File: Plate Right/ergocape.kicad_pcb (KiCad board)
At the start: 2 copper layers, 183.2 x 140.8 mm, 43 parts

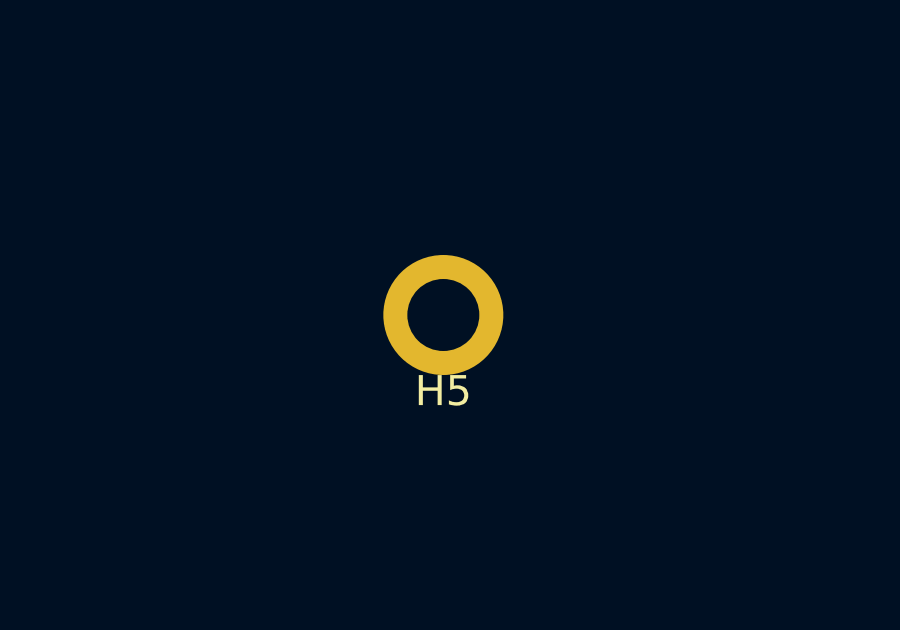
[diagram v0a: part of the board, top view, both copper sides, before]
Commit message: Change in layout and design, remove atmega32u4
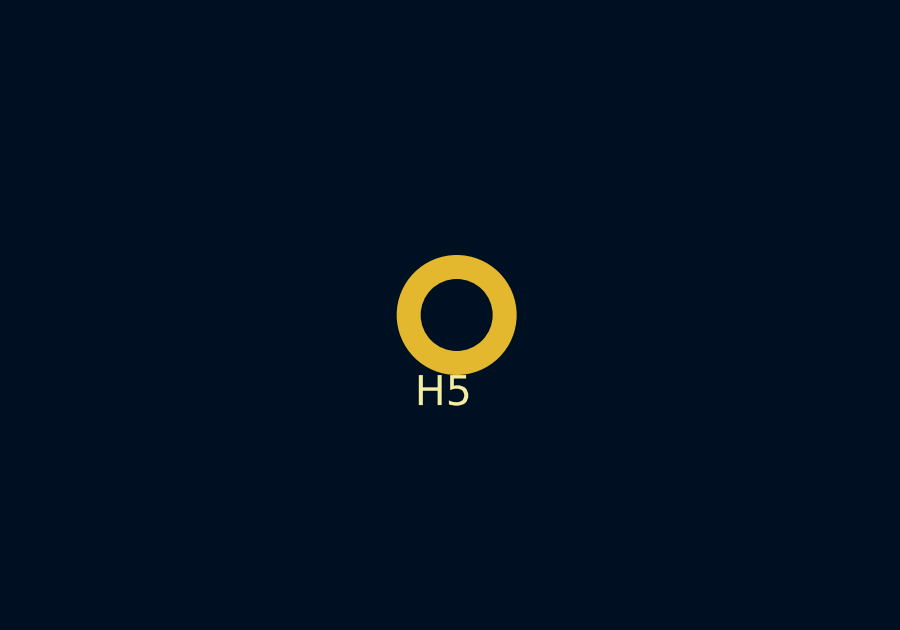
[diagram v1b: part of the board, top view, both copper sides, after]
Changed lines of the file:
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@@
     (mod_text_size 1 1)
     (mod_text_width 0.15)
-    (pad_size 5.2 5.2)
-    (pad_drill 4.7)
+    (pad_size 4 4)
+    (pad_drill 2.4)
     (pad_to_mask_clearance 0.051)
     (solder_mask_min_width 0.25)
@@
       (effects (font (size 1 1) (thickness 0.15)))
     )
-    (pad "" thru_hole circle (at 0 0) (size 4 4) (drill 2.4) (layers *.Cu *.Mask))
+    (pad "" thru_hole circle (at 0.4445 0) (size 4 4) (drill 2.4) (layers *.Cu *.Mask))
   )
   (module usbc_footprint:mount_hole_2.4x4 (layer F.Cu)

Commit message: cleanup and finish the case files
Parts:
- removed K_ESC1: KEYSW, acheron_SwitchSlots:slotMX100
- added K_BKSP_1: KEYSW, usbc_footprint:slotMX200, F.Cu at (55.6, 39.7)
- H1, H10, H11, H12, H2, H3, H5, H6, H8, H9: footprint usbc_footprint:mount_hole_2.4x4 -> acheron_MountingHoles:MountingHole_2.5x4.0mm
- K_1, K_2, K_3, K_4, K_5, K_A1, K_ALT1, K_B1, K_BOT_1U_1, K_BOT_1U_2, K_C1, K_CTRL1, K_D1, K_E1, K_F1, K_G1, K_Q1, K_R1, K_S1, K_T1, K_TAB1, K_THUMB_1U_3, K_THUMB_1U_4, K_TH_1U_1, K_TH_1U_2, K_V1, K_W1, K_WIN1, K_X1, K_Z1: footprint acheron_SwitchSlots:slotMX100 -> usbc_footprint:slotMX100
- K_ENTER_rev_2.25u_1, K_SHIFT_REV_2.75_1: footprint acheron_SwitchSlots:slotMX200 -> usbc_footprint:slotMX200
- moved H10 16.1 mm to (39.6, 60.5)
- moved H11 14.2 mm to (39.9, 20.2)
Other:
- outline, holes or cut-outs redrawn
